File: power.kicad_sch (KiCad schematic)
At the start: 11 parts, among them J27 USB_C_Receptacle_USB2.0_14P, U20 XC6206PxxxMR-G, U21 XC6206PxxxMR-G, U22 CH224K

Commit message: Small aesthetic changes and small rework of power sheet.
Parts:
- removed U20, U21: XC6206PxxxMR-G, Package_TO_SOT_SMD:SOT-23-3, symbol Regulator_Linear:XC6206PxxxMR
- added C25, C26: 22u, symbol Device:C
- added C40: 1u, symbol Device:C
- added C41: 100n, symbol Device:C
- added J28: USB_C_Receptacle_USB2.0_14P, symbol Connector:USB_C_Receptacle_USB2.0_14P
- added L1: 15u, symbol Device:L
- added R10: 105K, symbol Device:R
- added R11: 49.9, symbol Device:R
- added R12: 100K, symbol Device:R
- added R13: 13.3K, symbol Device:R
- added R6: 0, symbol Device:R
- added R7: 1K, symbol Device:R
- added R8: 10K, symbol Device:R
- added R9: 511K, symbol Device:R
- added U2: CH224K, Package_SO:SSOP-10-1EP_3.9x4.9mm_P1mm_EP2.1x3.3mm, symbol Interface_USB:CH224K
- added U3: TPS54202DDC, Package_TO_SOT_SMD:SOT-23-6, symbol Regulator_Switching:TPS54202DDC
- C13: value 10u -> 1u
- C14: value 1u -> 100n
- C15: value 1u -> 22u
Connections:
- net +1V2 is gone; now on net +5V: C15.1
- net +5V: now also C25.1, L1.2, R11.1; no longer C13.1, R5.1
- net GND: now also U22.3 (CFG3), U22.9 (CFG1), C25.2, C40.2, C41.2, J28.A1 (GND), J28.A12 (GND), J28.B1 (GND), J28.B12 (GND), J28.S1 (SHIELD), R10.2, R13.2, U2.11 (GND), U2.3 (CFG3), U2.9 (CFG1), U3.1 (GND); no longer C14.2
- net VBUS: now also J28.A4 (VBUS), J28.A9 (VBUS), J28.B4 (VBUS), J28.B9 (VBUS), R6.2, R7.1, R8.1
- net at C37.1, R3.2, U22.1 (VDD): now also U22.2 (CFG2); no longer U22.9 (CFG1)
- net +3V3: no longer names the net of C14.1
- net +3V3: now also U3.6 (BOOT)
- new net: C26.1, R11.2, R12.1
- new net: C26.2, R12.2, R13.1, U3.4 (FB)
- new net: C13.1, R7.2, U2.1 (VDD), U2.2 (CFG2)
- new net: C14.2, L1.1, U3.2 (SW)
- new net: J28.A5 (CC1), U2.7 (CC1)
- new net: J28.A6 (D+), J28.B6 (D+), U2.4 (DP)
- new net: J28.A7 (D-), J28.B7 (D-), U2.5 (DM)
- new net: J28.B5 (CC2), U2.6 (CC2)
- new net: R8.2, U2.8 (VBUS)
- new net: R10.1, R9.1, U3.5 (EN)
- new net +20V: C40.1, C41.1, R5.1, R6.1, R9.2, U3.3 (VIN)
- no-connect marks 3 -> 2
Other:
- moved on the sheet: C37, J27, R3, R4, R5, U22

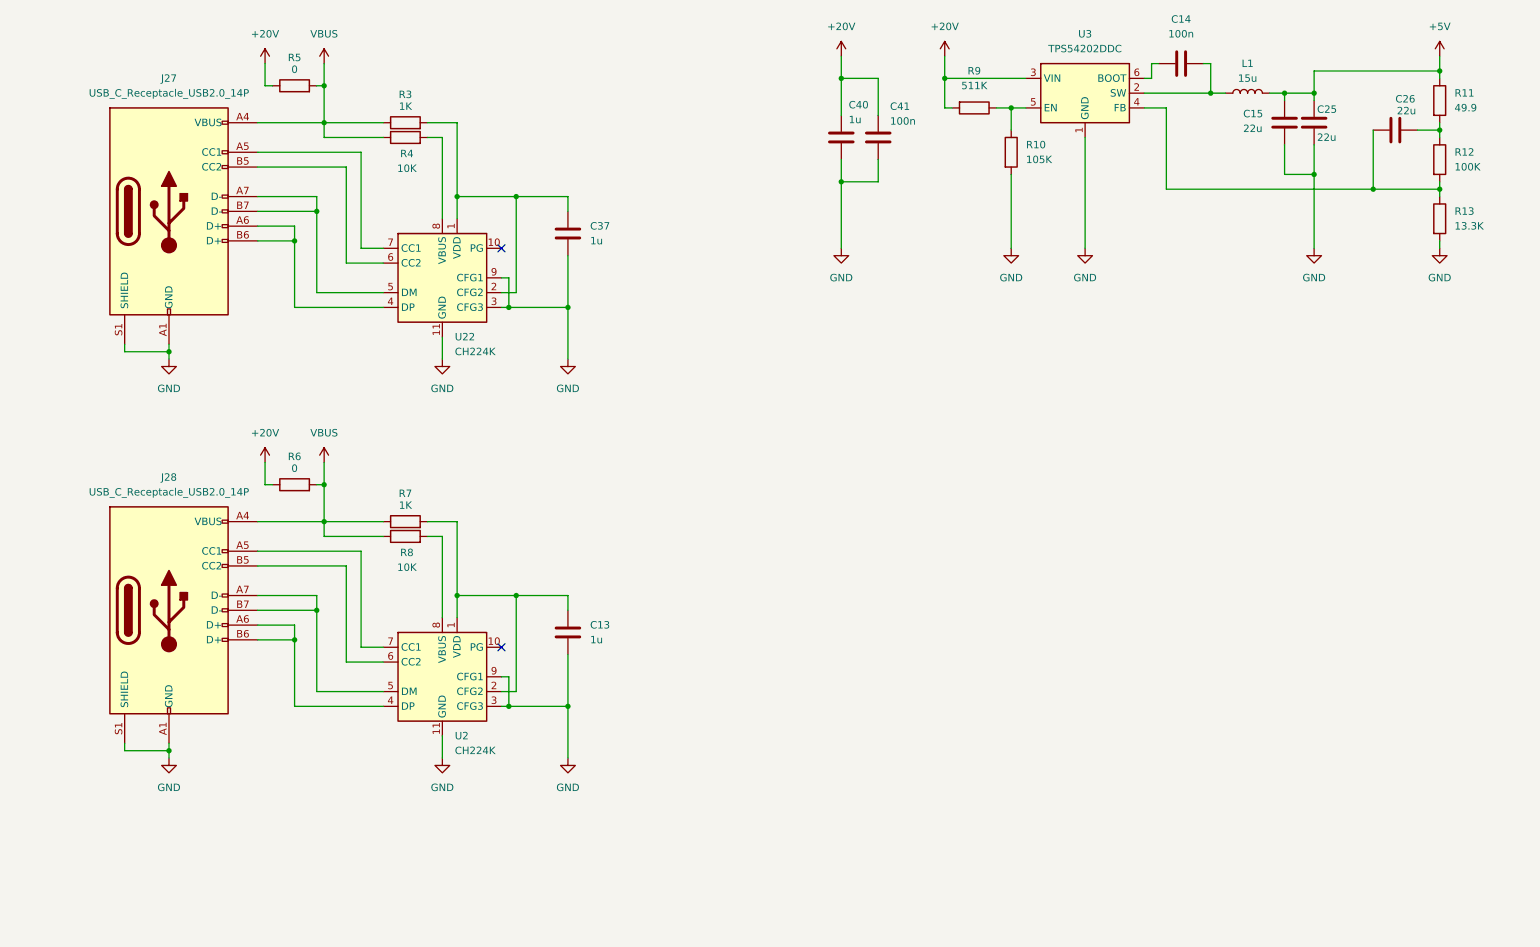
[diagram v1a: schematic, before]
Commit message: add power redundancy with OR-ing controller
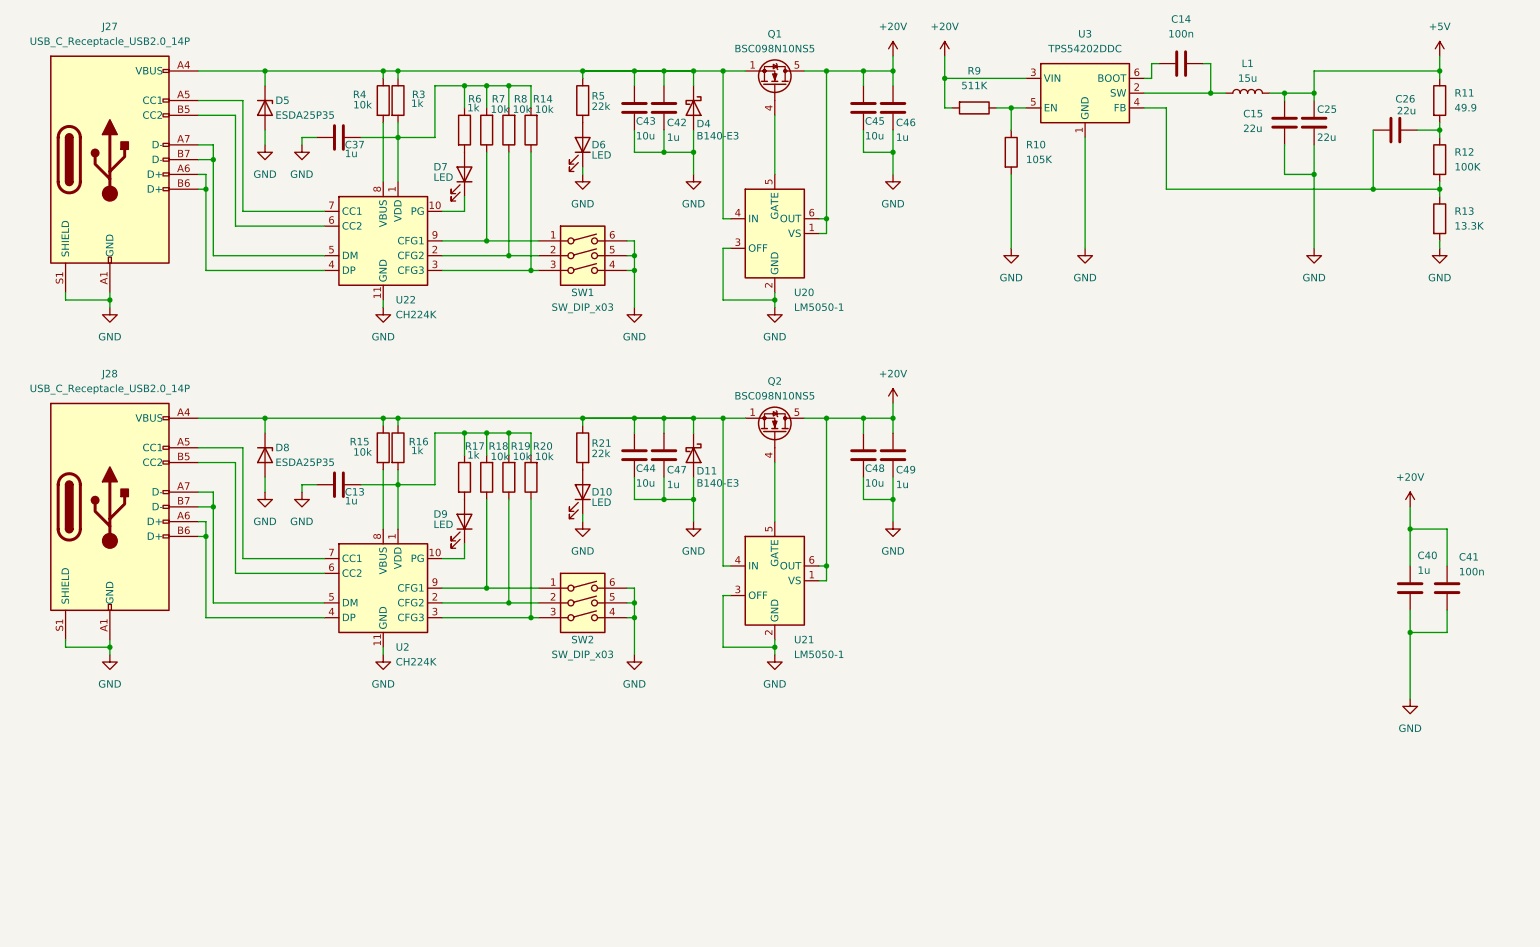
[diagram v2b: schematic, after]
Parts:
- added C42, C46, C47, C49: 1u, symbol Device:C
- added C43, C44, C45, C48: 10u, symbol Device:C
- added D10, D6, D7, D9: LED, symbol Device:LED
- added D11, D4: B140-E3, Diode_SMD:D_SMA, symbol Diode:B140-E3
- added D5, D8: ESDA25P35, symbol Device:D_Zener
- added Q1, Q2: BSC098N10NS5, Package_TO_SOT_SMD:TDSON-8-1, symbol Transistor_FET:BSC098N10NS5
- added R14, R15, R18, R19, R20: 10k, symbol Device:R
- added R16, R17: 1k, symbol Device:R
- added R21: 22k, symbol Device:R
- added SW1, SW2: SW_DIP_x03, symbol Switch:SW_DIP_x03
- added U20, U21: LM5050-1, Package_TO_SOT_SMD:TSOT-23-6, symbol Power_Management:LM5050-1
- R3: value 1K -> 1k
- R4, R8: value 10K -> 10k
- R5: value 0 -> 22k
- R6: value 0 -> 1k
- R7: value 1K -> 10k
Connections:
- net +20V: now also C45.1, C46.1, C48.1, C49.1, Q1.5 (D), Q2.5 (D), U20.1 (VS), U20.6 (OUT), U21.1 (VS), U21.6 (OUT); no longer R5.1, R6.1
- net GND: now also C42.2, C43.2, C44.2, C45.2, C46.2, C47.2, C48.2, C49.2, D10.1 (K), D11.2 (A), D4.2 (A), D5.2 (A), D6.1 (K), D8.2 (A), SW1.4, SW1.5, SW1.6, SW2.4, SW2.5, SW2.6, U20.2 (GND), U20.3 (OFF), U21.2 (GND), U21.3 (OFF); no longer U2.3 (CFG3), U2.9 (CFG1), U22.3 (CFG3), U22.9 (CFG1)
- net at C13.1, U2.1 (VDD): now also R16.2, R17.1, R18.2, R19.2, R20.2; no longer R7.2, U2.2 (CFG2)
- net at C37.1, R3.2, U22.1 (VDD): now also R6.1, R7.2, R8.2, R14.2; no longer U22.2 (CFG2)
- net at U22.10 (PG): now also D7.1 (K)
- net at U2.8 (VBUS): now also R15.2; no longer R8.2
- net at U2.10 (PG): now also D9.1 (K)
- removed net VBUS: J27.A4 (VBUS), J27.A9 (VBUS), J27.B4 (VBUS), J27.B9 (VBUS), J28.A4 (VBUS), J28.A9 (VBUS), J28.B4 (VBUS), J28.B9 (VBUS), R3.1, R4.1, R5.2, R6.2, R7.1, R8.1
- new net: C44.1, C47.1, D11.1 (K), D8.1 (K), J28.A4 (VBUS), J28.A9 (VBUS), J28.B4 (VBUS), J28.B9 (VBUS), Q2.1 (S), Q2.2 (S), Q2.3 (S), R15.1, R16.1, R21.1, U21.4 (IN)
- new net: R19.1, SW2.2, U2.2 (CFG2)
- new net: R20.1, SW2.3, U2.3 (CFG3)
- new net: R18.1, SW2.1, U2.9 (CFG1)
- new net: C42.1, C43.1, D4.1 (K), D5.1 (K), J27.A4 (VBUS), J27.A9 (VBUS), J27.B4 (VBUS), J27.B9 (VBUS), Q1.1 (S), Q1.2 (S), Q1.3 (S), R3.1, R4.1, R5.1, U20.4 (IN)
- new net: D10.2 (A), R21.2
- new net: R8.1, SW1.2, U22.2 (CFG2)
- new net: R14.1, SW1.3, U22.3 (CFG3)
- new net: R7.1, SW1.1, U22.9 (CFG1)
- new net: Q1.4 (G), U20.5 (GATE)
- new net: D7.2 (A), R6.2
- new net: D6.2 (A), R5.2
- new net: D9.2 (A), R17.2
- new net: Q2.4 (G), U21.5 (GATE)
- no-connect marks 2 -> 0
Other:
- moved on the sheet: C37, C40, C41, J27, R3, R4, U22

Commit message: complete power
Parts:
- removed C13, C37, C40, C42, C46, C47, C49: 1u, symbol Device:C
- removed C41: 100n, symbol Device:C
- removed C43, C44, C45, C48: 10u, symbol Device:C
- removed D10, D6, D7, D9: LED, symbol Device:LED
- removed D11, D4: B140-E3, Diode_SMD:D_SMA, symbol Diode:B140-E3
- removed D5, D8: ESDA25P35, symbol Device:D_Zener
- removed J27, J28: USB_C_Receptacle_USB2.0_14P, symbol Connector:USB_C_Receptacle_USB2.0_14P
- removed L1: 15u, symbol Device:L
- removed Q1, Q2: BSC098N10NS5, Package_TO_SOT_SMD:TDSON-8-1, symbol Transistor_FET:BSC098N10NS5
- removed R11: 49.9, symbol Device:R
- removed R12: 100K, symbol Device:R
- removed R13: 13.3K, symbol Device:R
- removed R14, R15, R18, R19, R20, R4, R7, R8: 10k, symbol Device:R
- removed R16, R17, R3, R6: 1k, symbol Device:R
- removed R21, R5: 22k, symbol Device:R
- removed SW1, SW2: SW_DIP_x03, symbol Switch:SW_DIP_x03
- removed U2, U22: CH224K, Package_SO:SSOP-10-1EP_3.9x4.9mm_P1mm_EP2.1x3.3mm, symbol Interface_USB:CH224K
- removed U20, U21: LM5050-1, Package_TO_SOT_SMD:TSOT-23-6, symbol Power_Management:LM5050-1
- removed U3: TPS54202DDC, Package_TO_SOT_SMD:SOT-23-6, symbol Regulator_Switching:TPS54202DDC
- added C50, C84, C87: 10u, Capacitor_SMD:C_1206_3216Metric, symbol Device:C
- added C51, C52: 100n, Capacitor_SMD:C_0402_1005Metric, symbol Device:C
- added C53: 47p, Capacitor_SMD:C_0402_1005Metric, symbol Device:C
- added C54, C55: 22u, Capacitor_SMD:C_0603_1608Metric, symbol Device:C
- added C82, C83, C85, C86: 1u, Capacitor_SMD:C_0603_1608Metric, symbol Device:C
- added L2: 10uH, Inductor_SMD:L_Changjiang_FXL0530, symbol Device:L
- added R23: 10k, Resistor_SMD:R_0402_1005Metric, symbol Device:R
- added R24: 1k, Resistor_SMD:R_0402_1005Metric, symbol Device:R
- added R34: 100k, Resistor_SMD:R_0402_1005Metric, symbol Device:R
- added R38: 220k, symbol Device:R
- added R39: 47k, symbol Device:R
- added U23: TPS54302, Package_TO_SOT_SMD:SOT-23-6, symbol Regulator_Switching:TPS54302
- added U28, U29: TPS7A4701, Package_DFN_QFN:Texas_RGW0020A_VQFN-20-1EP_5x5mm_P0.65mm_EP3.15x3.15mm_ThermalVias, symbol tps7a4701:TPS7A4701xRGW
- added U3: TPS7A7002DDA, Package_SO:TI_SO-PowerPAD-8, symbol Regulator_Linear:TPS7A7001DDA
- C14: value 100n -> 10u; footprint (none) -> Capacitor_SMD:C_1206_3216Metric; LCSC (none) -> C13585
- C15, C26: value 22u -> 100n
- C25: value 22u -> 10u; footprint (none) -> Capacitor_SMD:C_1206_3216Metric; LCSC (none) -> C13585
- R10: value 105K -> 33k
- R9: value 511K -> 47k
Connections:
- net +20V: now also C50.1, C51.2, R38.1, U23.3 (VIN); no longer R9.2
- net +5V: now also C84.1, U28.1 (OUT), U28.20 (OUT), U28.3 (SENSE/FB); no longer C15.1, C25.1
- net GND: now also C14.2, C26.2, C50.2, C51.1, C54.1, C55.1, C82.2, C83.2, C84.2, C85.2, C86.2, C87.2, R24.1, R39.1, U23.1 (GND), U28.10 (0.4V), U28.17 (NC), U28.18 (NC), U28.19 (NC), U28.2 (NC), U28.21 (EP), U28.6 (3.2V), U28.7 (GND), U29.11 (0.2V), U29.12 (0.1V), U29.17 (NC), U29.18 (NC), U29.19 (NC), U29.2 (NC), U29.21 (EP), U29.7 (GND), U29.8 (1.6V), U3.8 (GND), U3.9 (EP)
- net +1V2: now reaches C26.1
- net +1V2: now also C25.1, R9.1, U3.6 (OUT)
- net +6V: now reaches C14.1
- net +6V: now also C15.1, C53.2, C54.2, C55.2, C82.1, C85.1, L2.2, R34.2, U28.13 (EN), U28.15 (IN), U28.16 (IN), U29.13 (EN), U29.15 (IN), U29.16 (IN), U3.2 (EN), U3.3 (IN)
- net at R10.1: now also R9.2, U3.7 (FB); no longer R9.1
- new net: C86.1, U29.14 (NR)
- new net: R23.2, R24.2
- new net: C83.1, U28.14 (NR)
- new net: C52.2, L2.1, U23.2 (SW)
- new net: C53.1, R23.1, R34.1, U23.4 (FB)
- new net: R38.2, R39.2, U23.5 (EN)
- new net: C52.1, U23.6 (BOOT)
- new net +3V3: C87.1, U29.1 (OUT), U29.20 (OUT), U29.3 (SENSE/FB)
- no-connect marks 0 -> 11

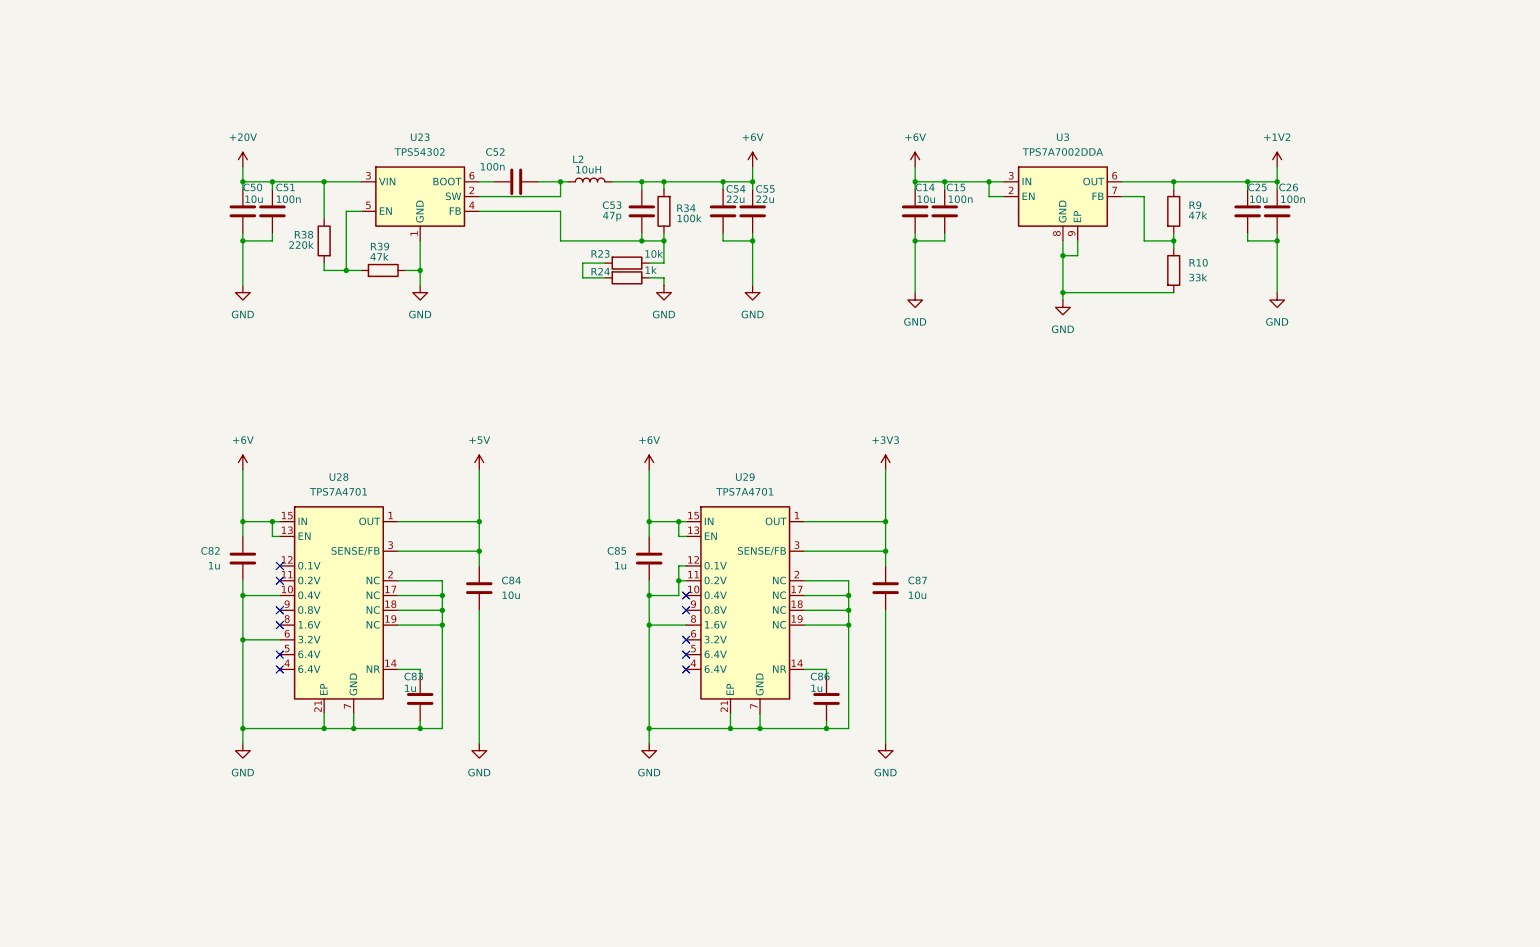
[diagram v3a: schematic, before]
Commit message: reroute dac + comparators
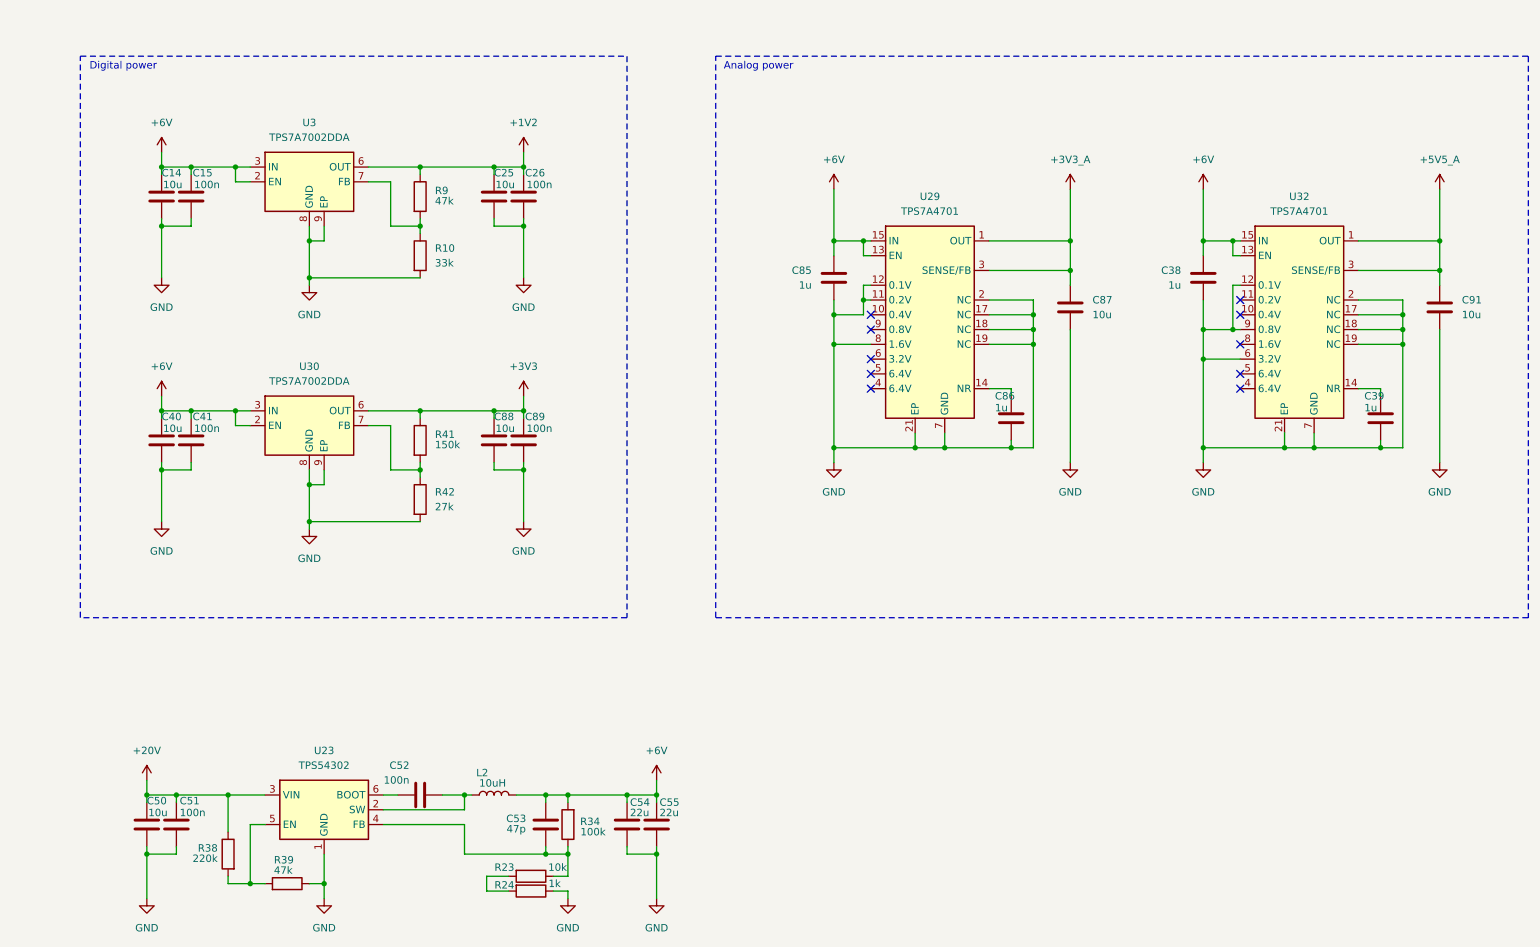
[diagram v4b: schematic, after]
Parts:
- removed C82, C83: 1u, Capacitor_SMD:C_0603_1608Metric, symbol Device:C
- removed C84: 10u, Capacitor_SMD:C_1206_3216Metric, symbol Device:C
- removed U28: TPS7A4701, Package_DFN_QFN:Texas_RGW0020A_VQFN-20-1EP_5x5mm_P0.65mm_EP3.15x3.15mm_ThermalVias, symbol tps7a4701:TPS7A4701xRGW
- added C38, C39: 1u, Capacitor_SMD:C_0603_1608Metric, symbol Device:C
- added C40, C88, C91: 10u, Capacitor_SMD:C_1206_3216Metric, symbol Device:C
- added C41, C89: 100n, symbol Device:C
- added R41: 150k, symbol Device:R
- added R42: 27k, symbol Device:R
- added U30: TPS7A7002DDA, Package_SO:TI_SO-PowerPAD-8, symbol Regulator_Linear:TPS7A7001DDA
- added U32: TPS7A4701, Package_DFN_QFN:Texas_RGW0020A_VQFN-20-1EP_5x5mm_P0.65mm_EP3.15x3.15mm_ThermalVias, symbol tps7a4701:TPS7A4701xRGW
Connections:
- net +3V3: now also C88.1, C89.1, R41.1, U30.6 (OUT); no longer C87.1, U29.1 (OUT), U29.20 (OUT), U29.3 (SENSE/FB)
- net +6V: now also C38.1, C40.1, C41.1, U30.2 (EN), U30.3 (IN), U32.13 (EN), U32.15 (IN), U32.16 (IN)
- net GND: now also C38.2, C39.2, C40.2, C41.2, C88.2, C89.2, C91.2, R42.2, U30.8 (GND), U30.9 (EP), U32.12 (0.1V), U32.17 (NC), U32.18 (NC), U32.19 (NC), U32.2 (NC), U32.21 (EP), U32.6 (3.2V), U32.7 (GND), U32.9 (0.8V)
- new net: R41.2, R42.1, U30.7 (FB)
- new net: C39.1, U32.14 (NR)
- new net +3V3_A: C87.1, U29.1 (OUT), U29.20 (OUT), U29.3 (SENSE/FB)
- new net +5V5_A: C91.1, U32.1 (OUT), U32.20 (OUT), U32.3 (SENSE/FB)
- no-connect marks 11 -> 10
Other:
- note added: "Analog power"
- note added: "Digital power"
- moved on the sheet: C14, C15, C25, C26, C50, C51, C52, C53, C54, C55, C85, C86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
